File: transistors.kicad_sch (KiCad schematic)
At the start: 22 parts, among them J11 Transistor_2, J12 Transistor_1, J13 Transistor_4, J14 Transistor_.3, Q1 DMN2011UTS, Q2 DMN2011UTS, Q3 DMN2011UTS, Q4 DMN2011UTS, U6 MOCD20, U7 MOCD20

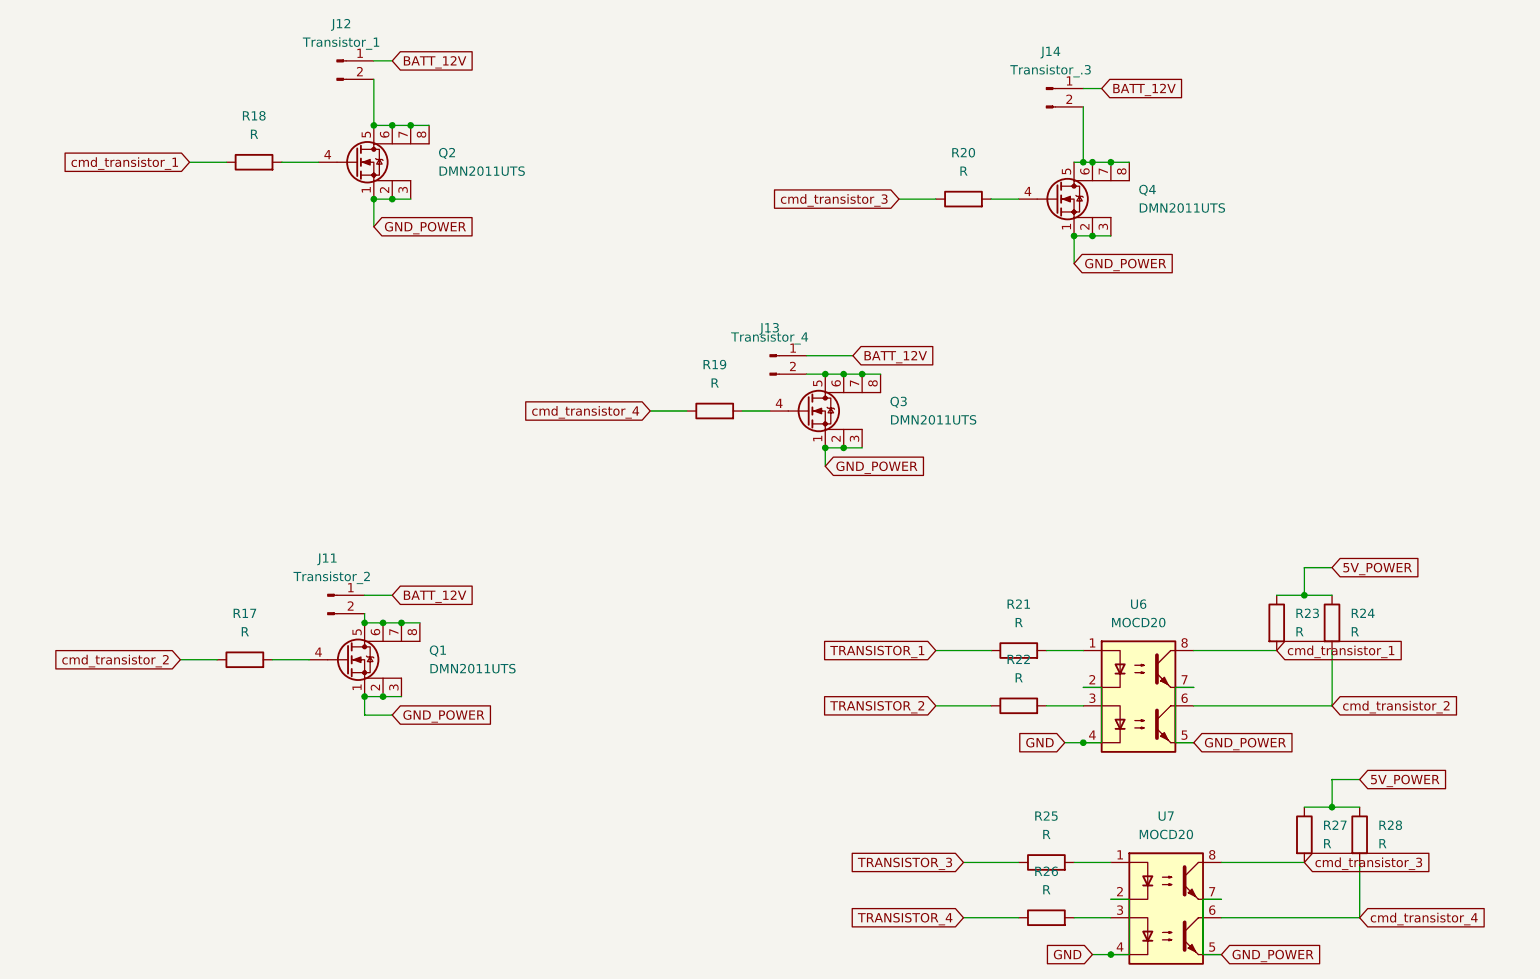
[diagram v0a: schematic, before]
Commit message: version without mega I2C pins
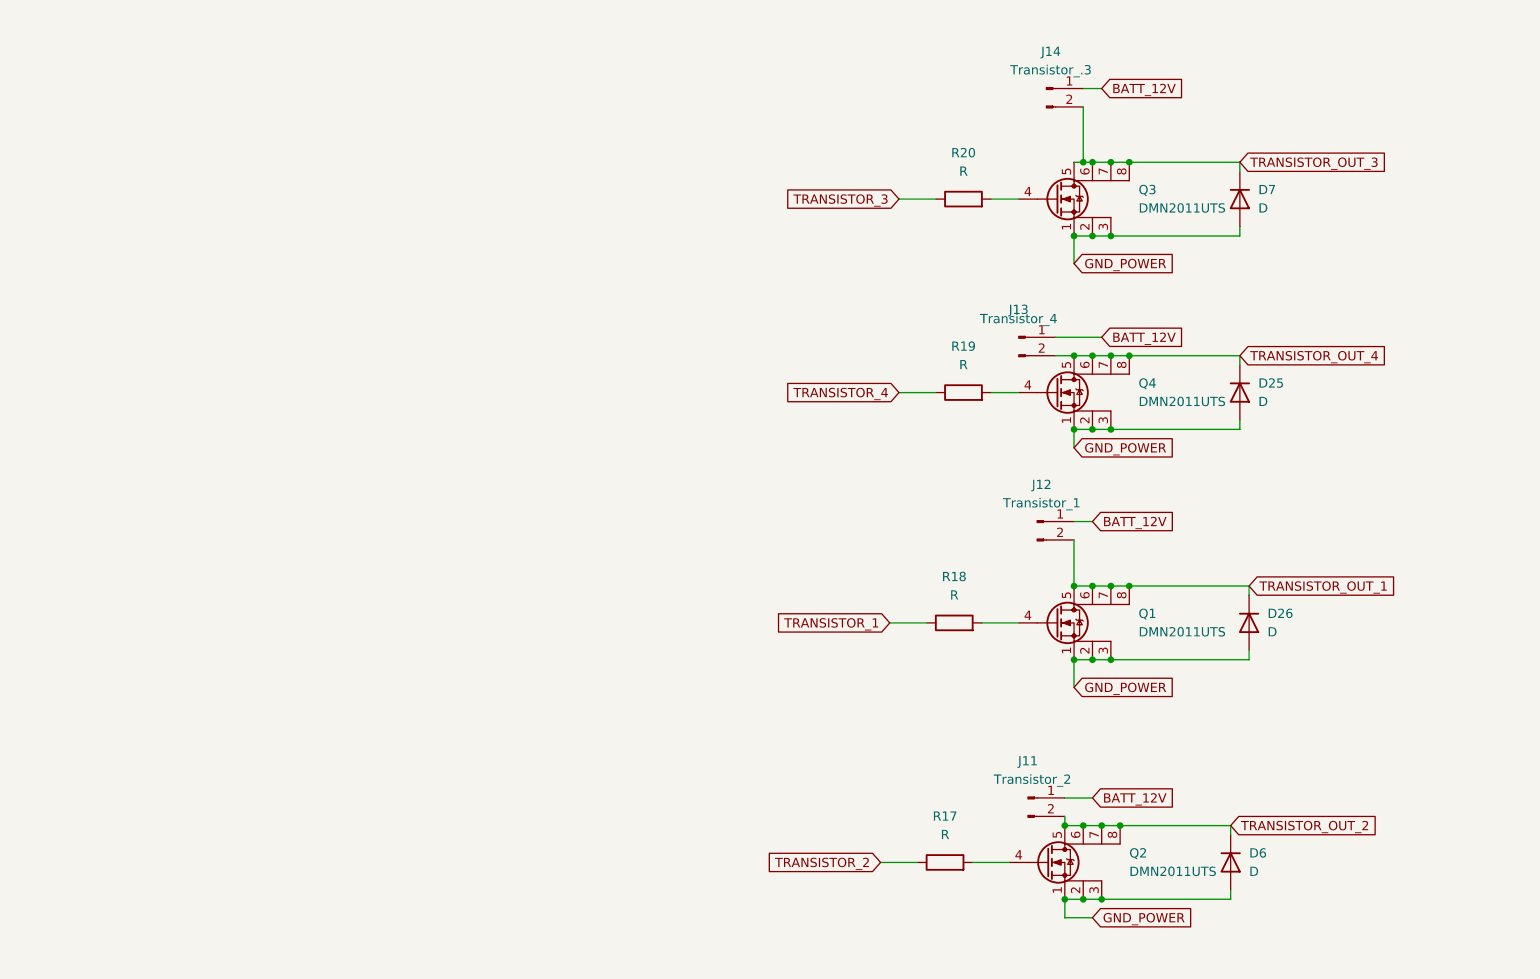
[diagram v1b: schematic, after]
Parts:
- removed R21, R22, R23, R24, R25, R26, R27, R28: R, Resistor_SMD:R_0603_1608Metric, symbol Device:R
- removed U6, U7: MOCD20, Package_SO:SO-8_3.9x4.9mm_P1.27mm, symbol New_Library_Victor:MOCD20
- added D25, D26, D6, D7: D, Diode_SMD:D_1206_3216Metric, symbol Device:D
- renumbered Q2 to Q1, Q1 to Q2, Q4 to Q3, Q3 to Q4
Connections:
- net cmd_transistor_1 is gone; now on net TRANSISTOR_1: R18.1
- net cmd_transistor_2 is gone; now on net TRANSISTOR_2: R17.1
- net cmd_transistor_3 is gone; now on net TRANSISTOR_3: R20.1
- net cmd_transistor_4 is gone; now on net TRANSISTOR_4: R19.1
- net GND_POWER: now also D25.2 (A), D26.2 (A), D6.2 (A), D7.2 (A)
- net TRANSISTOR_OUT_4: now reaches J13.2 (Pin_2), Q4.5 (D), Q4.6 (D), Q4.7 (D), Q4.8 (D)
- net TRANSISTOR_OUT_4: now also D25.1 (K)
- net TRANSISTOR_OUT_2: now reaches J11.2 (Pin_2), Q2.5 (D), Q2.6 (D), Q2.7 (D), Q2.8 (D)
- net TRANSISTOR_OUT_2: now also D6.1 (K)
- net TRANSISTOR_OUT_3: now reaches J14.2 (Pin_2), Q3.5 (D), Q3.6 (D), Q3.7 (D), Q3.8 (D)
- net TRANSISTOR_OUT_3: now also D7.1 (K)
- net TRANSISTOR_OUT_1: now reaches J12.2 (Pin_2), Q1.5 (D), Q1.6 (D), Q1.7 (D), Q1.8 (D)
- net TRANSISTOR_OUT_1: now also D26.1 (K)
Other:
- moved on the sheet: J11, J12, J13, Q1, Q2, Q4, R17, R18, R19

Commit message: small fixes
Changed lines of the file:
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@@
     )
   )
-  (global_label "TRANSISTOR_OUT_1" (shape input) (at 213.36 109.22 0) (fields_autoplaced)
+  (global_label "TRANSISTOR_OUT_1" (shape output) (at 213.36 109.22 0) (fields_autoplaced)
     (effects (font (size 1.27 1.27)) (justify left))
     (property "Intersheet References" "${INTERSHEET_REFS}" (id 0) (at 233.795 109.1406 0)
@@
     )
   )
-  (global_label "TRANSISTOR_OUT_2" (shape input) (at 210.82 142.24 0) (fields_autoplaced)
+  (global_label "TRANSISTOR_OUT_2" (shape output) (at 210.82 142.24 0) (fields_autoplaced)
     (effects (font (size 1.27 1.27)) (justify left))
     (property "Intersheet References" "${INTERSHEET_REFS}" (id 0) (at 231.255 142.1606 0)
@@
     )
   )
-  (global_label "TRANSISTOR_OUT_3" (shape input) (at 212.09 50.8 0) (fields_autoplaced)
+  (global_label "TRANSISTOR_OUT_3" (shape output) (at 212.09 50.8 0) (fields_autoplaced)
     (effects (font (size 1.27 1.27)) (justify left))
     (property "Intersheet References" "${INTERSHEET_REFS}" (id 0) (at 232.525 50.7206 0)
@@
     )
   )
-  (global_label "TRANSISTOR_OUT_4" (shape input) (at 212.09 77.47 0) (fields_autoplaced)
+  (global_label "TRANSISTOR_OUT_4" (shape output) (at 212.09 77.47 0) (fields_autoplaced)
     (effects (font (size 1.27 1.27)) (justify left))
     (property "Intersheet References" "${INTERSHEET_REFS}" (id 0) (at 232.525 77.3906 0)

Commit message: JST_PH=>JST_XH. Version envoyee en fab
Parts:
- J11, J12, J13, J14: footprint Connector_JST:JST_PH_B2B-PH-K_1x02_P2.00mm_Vertical -> Connector_JST:JST_XH_B2B-XH-A_1x02_P2.50mm_Vertical
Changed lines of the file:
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@@
     (property "Reference" "J13" (id 0) (at 181.61 71.12 0))
     (property "Value" "Transistor_4" (id 1) (at 181.61 72.39 0))
-    (property "Footprint" "Connector_JST:JST_PH_B2B-PH-K_1x02_P2.00mm_Vertical" (id 2) (at 181.61 74.93 0)
+    (property "Footprint" "Connector_JST:JST_XH_B2B-XH-A_1x02_P2.50mm_Vertical" (id 2) (at 181.61 74.93 0)
       (effects (font (size 1.27 1.27)) hide)
     )
@@
     (property "Reference" "J11" (id 0) (at 182.88 133.35 0))
     (property "Value" "Transistor_2" (id 1) (at 183.515 135.89 0))
-    (property "Footprint" "Connector_JST:JST_PH_B2B-PH-K_1x02_P2.00mm_Vertical" (id 2) (at 182.88 138.43 0)
+    (property "Footprint" "Connector_JST:JST_XH_B2B-XH-A_1x02_P2.50mm_Vertical" (id 2) (at 182.88 138.43 0)
       (effects (font (size 1.27 1.27)) hide)
     )
@@
     (property "Reference" "J14" (id 0) (at 186.055 35.56 0))
     (property "Value" "Transistor_.3" (id 1) (at 186.055 38.1 0))
-    (property "Footprint" "Connector_JST:JST_PH_B2B-PH-K_1x02_P2.00mm_Vertical" (id 2) (at 185.42 40.64 0)
+    (property "Footprint" "Connector_JST:JST_XH_B2B-XH-A_1x02_P2.50mm_Vertical" (id 2) (at 185.42 40.64 0)
       (effects (font (size 1.27 1.27)) hide)
     )
@@
     (property "Reference" "J12" (id 0) (at 184.785 95.25 0))
     (property "Value" "Transistor_1" (id 1) (at 184.785 97.79 0))
-    (property "Footprint" "Connector_JST:JST_PH_B2B-PH-K_1x02_P2.00mm_Vertical" (id 2) (at 184.15 100.33 0)
-      (effects (font (size 1.27 1.27)) hide)
-    )
+    (property "Footprint" "Connector_JST:JST_XH_B2B-XH-A_1x02_P2.50mm_Vertical" (id 2) (at 184.15 100.33 0)
+      (effects (font (size 1.27 1.27)) hide)
+    )

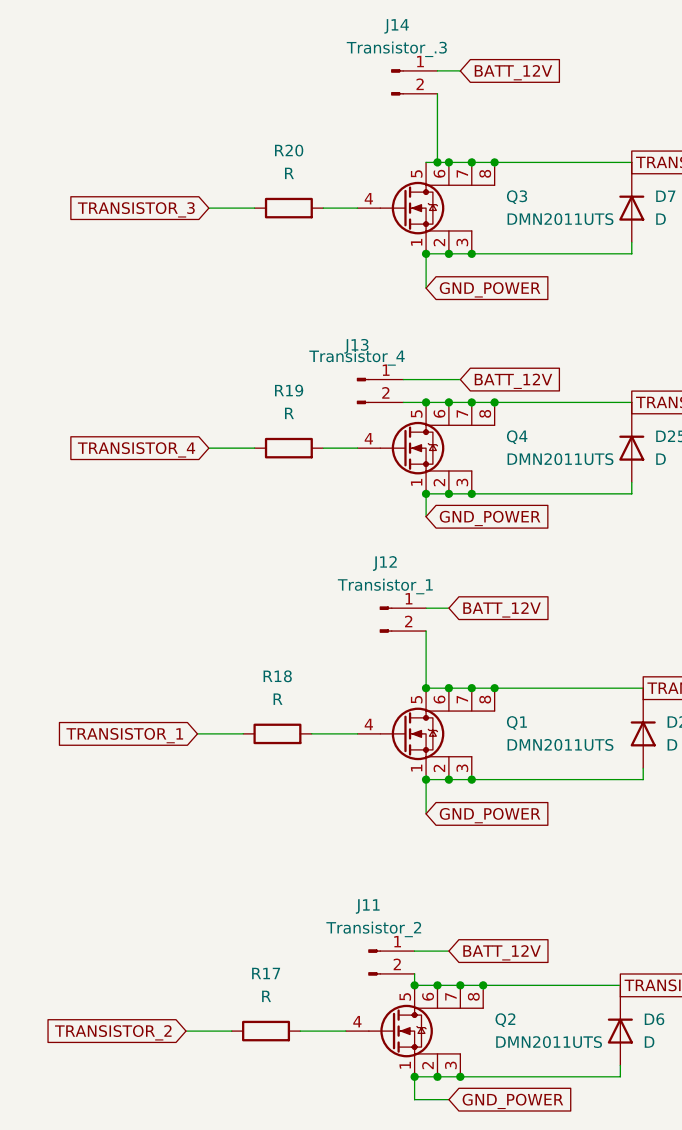
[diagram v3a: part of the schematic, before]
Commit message: specify values + BOM
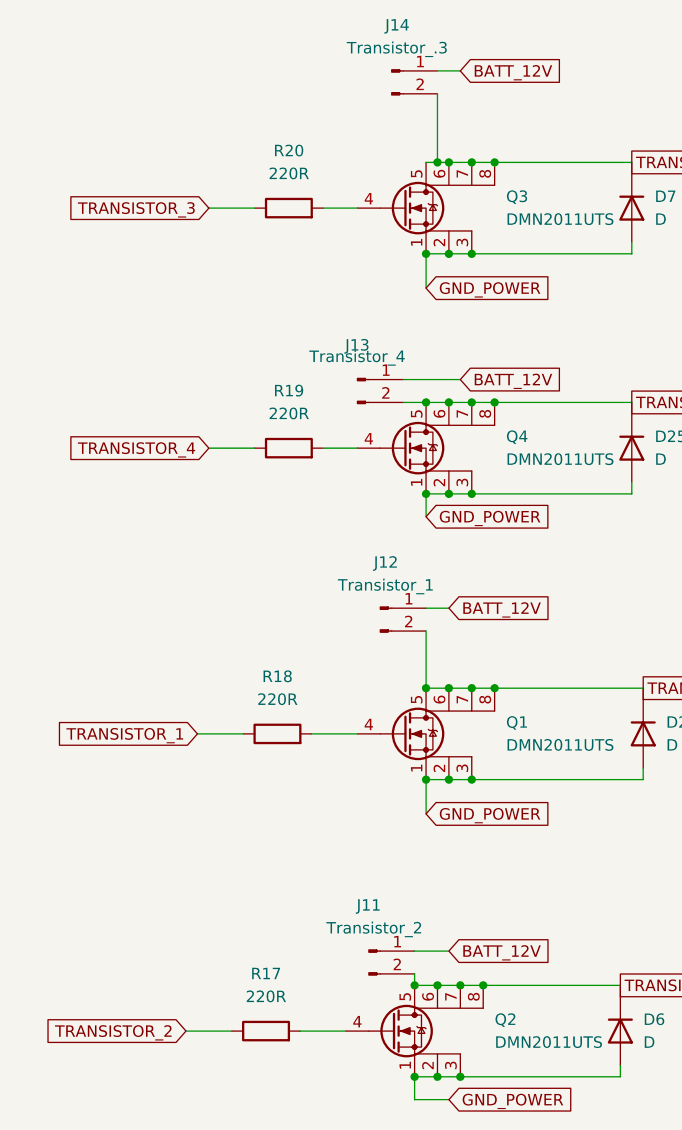
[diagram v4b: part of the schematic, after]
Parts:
- R17, R18, R19, R20: value R -> 220R
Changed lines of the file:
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@@
     (in_bom yes) (on_board yes) (fields_autoplaced)
     (property "Reference" "R17" (id 0) (at 171.45 140.97 90))
-    (property "Value" "R" (id 1) (at 171.45 143.51 90))
+    (property "Value" "220R" (id 1) (at 171.45 143.51 90))
     (property "Footprint" "Resistor_SMD:R_0603_1608Metric" (id 2) (at 171.45 149.098 90)
       (effects (font (size 1.27 1.27)) hide)
@@
     (in_bom yes) (on_board yes) (fields_autoplaced)
     (property "Reference" "R19" (id 0) (at 173.99 76.2 90))
-    (property "Value" "R" (id 1) (at 173.99 78.74 90))
+    (property "Value" "220R" (id 1) (at 173.99 78.74 90))
     (property "Footprint" "Resistor_SMD:R_0603_1608Metric" (id 2) (at 173.99 84.328 90)
       (effects (font (size 1.27 1.27)) hide)
@@
     (in_bom yes) (on_board yes) (fields_autoplaced)
     (property "Reference" "R20" (id 0) (at 173.99 49.53 90))
-    (property "Value" "R" (id 1) (at 173.99 52.07 90))
+    (property "Value" "220R" (id 1) (at 173.99 52.07 90))
     (property "Footprint" "Resistor_SMD:R_0603_1608Metric" (id 2) (at 173.99 57.658 90)
       (effects (font (size 1.27 1.27)) hide)
@@
     (in_bom yes) (on_board yes) (fields_autoplaced)
     (property "Reference" "R18" (id 0) (at 172.72 107.95 90))
-    (property "Value" "R" (id 1) (at 172.72 110.49 90))
+    (property "Value" "220R" (id 1) (at 172.72 110.49 90))
     (property "Footprint" "Resistor_SMD:R_0603_1608Metric" (id 2) (at 172.72 116.078 90)
       (effects (font (size 1.27 1.27)) hide)

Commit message: fix warnings + add internal layers + add Uart to steppers (TX only
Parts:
- J11, J12, J13, J14: symbol Connector:Conn_01x02_Male -> Connector:Conn_01x02_Pin
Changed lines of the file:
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@@
 	)
 	(symbol
-		(lib_id "Connector:Conn_01x02_Male")
+		(lib_id "Connector:Conn_01x02_Pin")
 		(at 181.61 74.93 0)
 		(unit 1)
@@
 			)
 		)
-		(property "Description" ""
+		(property "Description" "Generic connector, single row, 01x02, script generated"
 			(at 181.61 74.93 0)
 			(effects
@@
 			)
 		)
-		(property "Description" ""
+		(property "Description" "Diode"
+			(at 213.36 114.3 0)
+			(effects
+				(font
+					(size 1.27 1.27)
+				)
+				(hide yes)
+			)
+		)
+		(property "Sim.Device" "D"
+			(at 213.36 114.3 0)
+			(effects
+				(font
+					(size 1.27 1.27)
+				)
+				(hide yes)
+			)
+		)
+		(property "Sim.Pins" "1=K 2=A"
 			(at 213.36 114.3 0)
 			(effects
@@
 			)
 		)
-		(property "Description" ""
+		(property "Description" "Diode"
+			(at 210.82 147.32 0)
+			(effects
+				(font
+					(size 1.27 1.27)
+				)
+				(hide yes)
+			)
+		)
+		(property "Sim.Device" "D"
+			(at 210.82 147.32 0)
+			(effects
+				(font
+					(size 1.27 1.27)
+				)
+				(hide yes)
+			)
+		)
+		(property "Sim.Pins" "1=K 2=A"
 			(at 210.82 147.32 0)
 			(effects
@@
 			)
 		)
-		(property "Description" ""
+		(property "Description" "Diode"
+			(at 212.09 82.55 0)
+			(effects
+				(font
+					(size 1.27 1.27)
+				)
+				(hide yes)
+			)
+		)
+		(property "Sim.Device" "D"
+			(at 212.09 82.55 0)
+			(effects
+				(font
+					(size 1.27 1.27)
+				)
+				(hide yes)
+			)
+		)
+		(property "Sim.Pins" "1=K 2=A"
 			(at 212.09 82.55 0)
 			(effects
@@
 	)
 	(symbol
-		(lib_id "Connector:Conn_01x02_Male")
+		(lib_id "Connector:Conn_01x02_Pin")
 		(at 182.88 138.43 0)
 		(unit 1)
@@
 			)
 		)
-		(property "Description" ""
+		(property "Description" "Generic connector, single row, 01x02, script generated"
 			(at 182.88 138.43 0)
 			(effects
@@
 	)
 	(symbol
-		(lib_id "Connector:Conn_01x02_Male")
+		(lib_id "Connector:Conn_01x02_Pin")
 		(at 185.42 40.64 0)
 		(unit 1)
@@
 			)
 		)
-		(property "Description" ""
+		(property "Description" "Generic connector, single row, 01x02, script generated"
 			(at 185.42 40.64 0)
 			(effects
@@
 			)
 		)
-		(property "Description" ""
+		(property "Description" "Diode"
+			(at 212.09 55.88 0)
+			(effects
+				(font
+					(size 1.27 1.27)
+				)
+				(hide yes)
+			)
+		)
+		(property "Sim.Device" "D"
+			(at 212.09 55.88 0)
+			(effects
+				(font
+					(size 1.27 1.27)
+				)
+				(hide yes)
+			)
+		)
+		(property "Sim.Pins" "1=K 2=A"
 			(at 212.09 55.88 0)
 			(effects
@@
 	)
 	(symbol
-		(lib_id "Connector:Conn_01x02_Male")
+		(lib_id "Connector:Conn_01x02_Pin")
 		(at 184.15 100.33 0)
 		(unit 1)
@@
 			)
 		)
-		(property "Description" ""
+		(property "Description" "Generic connector, single row, 01x02, script generated"
 			(at 184.15 100.33 0)
 			(effects
